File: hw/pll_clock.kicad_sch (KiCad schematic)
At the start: 21 parts, among them J7 BNC, U7 5P49V5925, Y1 25MHz

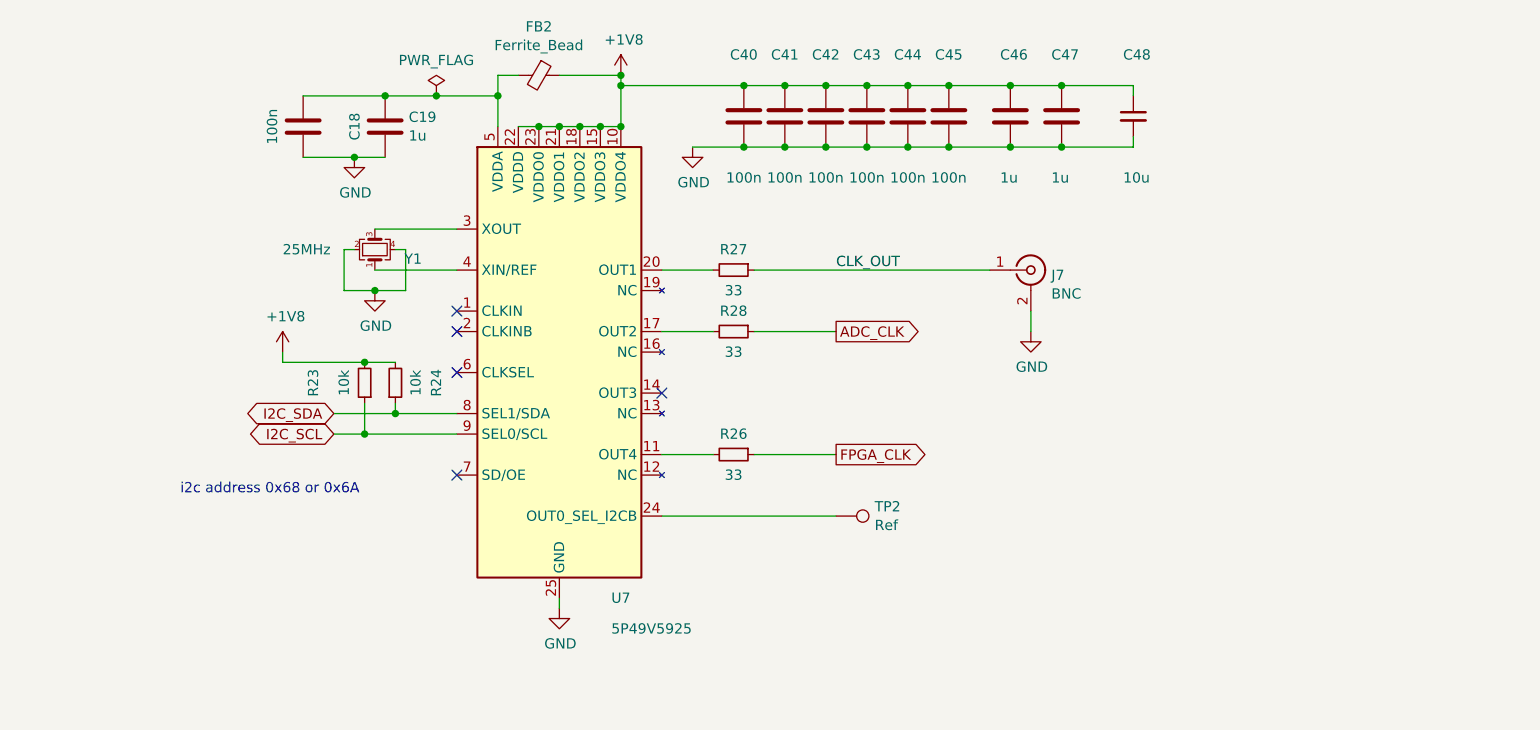
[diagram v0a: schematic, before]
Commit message: basic schematic, started layout (placing first components)
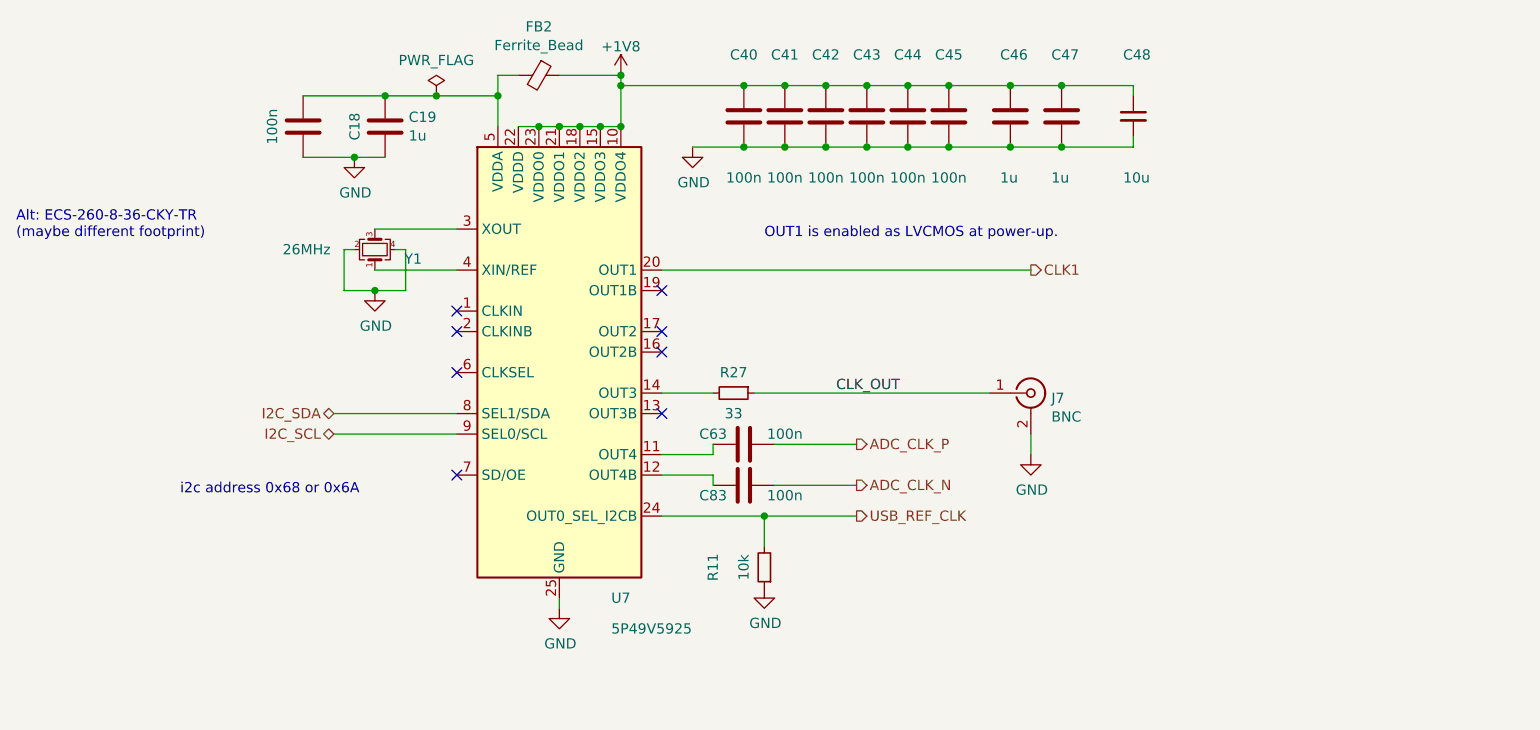
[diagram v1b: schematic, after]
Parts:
- removed R23, R24: 10k, Resistor_SMD:R_0603_1608Metric, symbol Device:R_Small
- removed R26, R28: 33, Resistor_SMD:R_0603_1608Metric, symbol Device:R_Small
- removed TP2: Ref, proj_footprints:TestPoint_Pad_D0.8mm_no_CY, symbol Connector:TestPoint
- added C63, C83: 100n, Capacitor_SMD:C_0603_1608Metric, symbol fmc:100nF_603
- added R11: 10k, Resistor_SMD:R_0603_1608Metric, symbol Device:R_Small
- FB2: symbol usbadc-rescue:Ferrite_Bead_Small-Device -> Device:FerriteBead_Small
- U7: symbol fmc:5P49V5925 -> Oscillator:5P49V6965
- Y1: value 25MHz -> 26MHz; Part ABM10W-25.0000MHZ-8-B1U-T3 -> ABM10W-26.0000MHZ-8-B1U-T3
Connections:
- net GND: now also R11.1
- net at R27.2: now also U7.14 (OUT3); no longer U7.20 (OUT1)
- net at U7.11 (OUT4): now also C63.2
- net at U7.12 (OUT4B): now also C83.2
- net USB_REF_CLK: now reaches U7.24 (OUT0_SEL_I2CB)
- net USB_REF_CLK: now also R11.2
- new net ADC_CLK_N: C83.1
- new net ADC_CLK_P: C63.1
- new net CLK1: U7.20 (OUT1)
- no-connect marks 5 -> 8
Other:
- note added: "Alt: ECS-260-8-36-CKY-TR (maybe different footprint)"
- note added: "OUT1 is enabled as LVCMOS at power-up."
- moved on the sheet: J7, R27

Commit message: WIP - a lot already laid out.
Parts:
- added R24: 33, Resistor_SMD:R_0603_1608Metric, symbol Device:R_Small
- added TP1: GND, usbadc_local:single_pad, symbol Connector:TestPoint_Small
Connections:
- net CLK1: now also R24.1; no longer U7.20 (OUT1)
- net GND: now also TP1.1
- net at R27.2: now also U7.17 (OUT2); no longer U7.14 (OUT3)
- net at U7.11 (OUT4): no longer C63.2
- net at U7.12 (OUT4B): no longer C83.2
- net at U7.13 (OUT3B): now also C83.2
- new net: C63.2, U7.14 (OUT3)
- new net: R24.2, U7.20 (OUT1)
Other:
- moved on the sheet: C63, C83, J7, R27

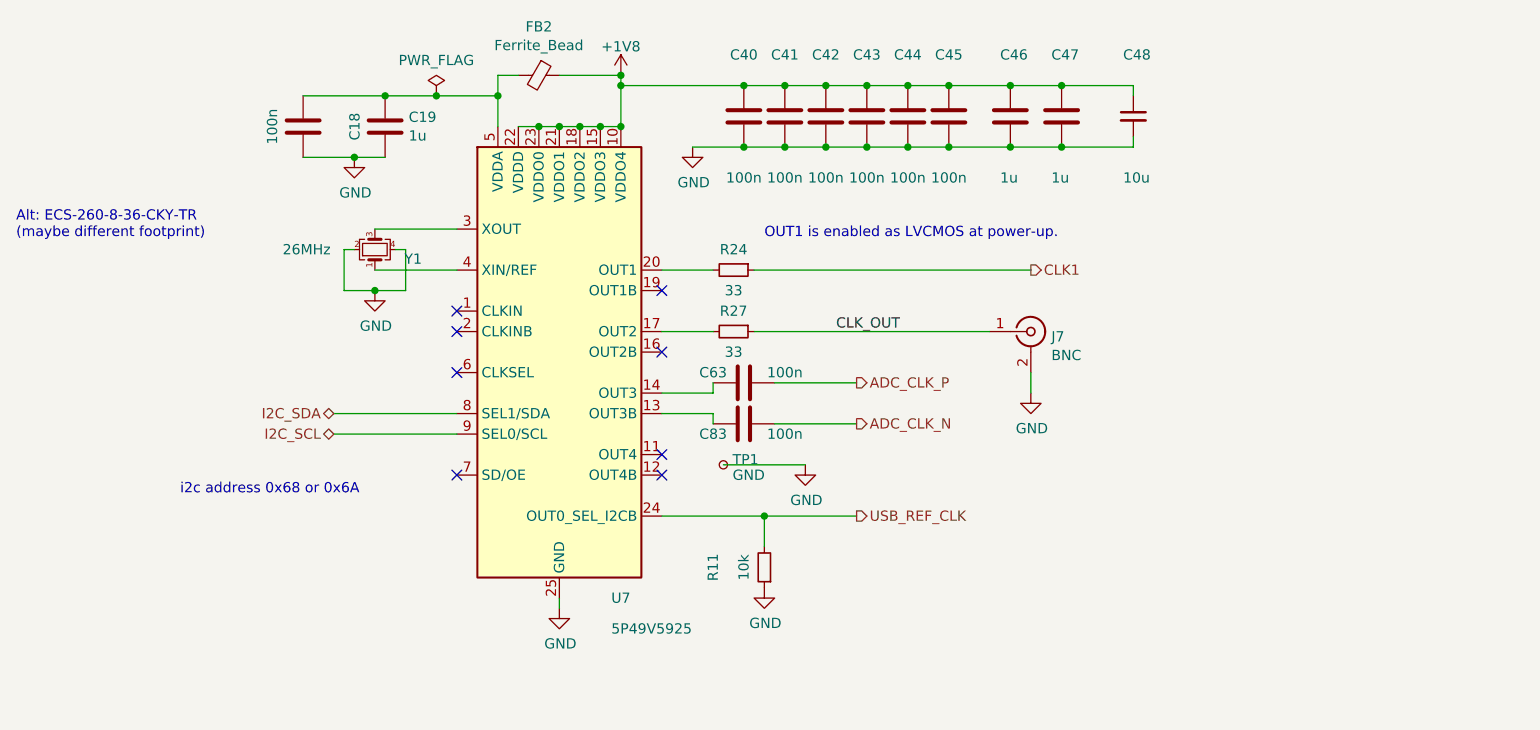
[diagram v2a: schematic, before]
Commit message: WIP - almost everything except power (converters) connected
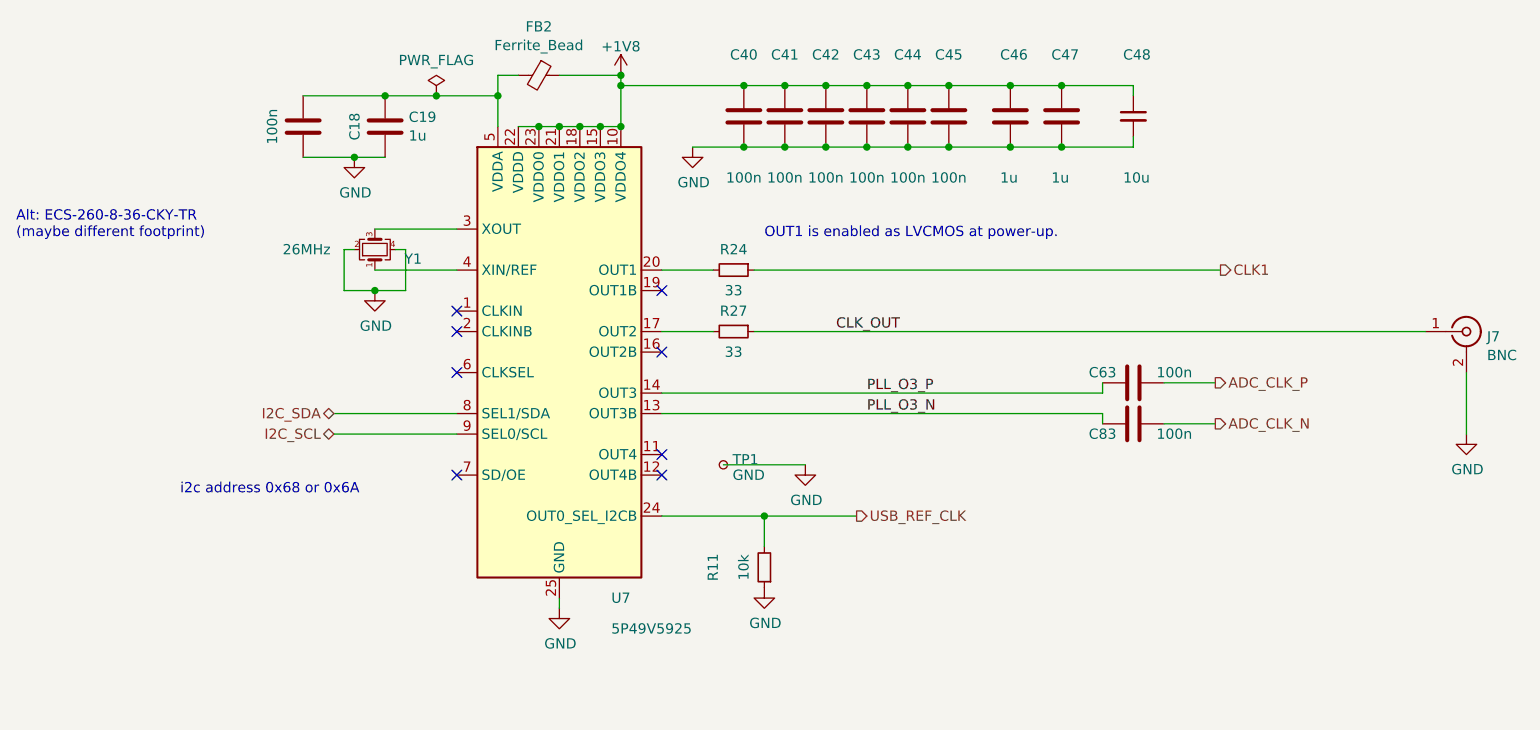
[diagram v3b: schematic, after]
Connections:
- net PLL_O3_N: now reaches C83.2, U7.13 (OUT3B)
- net PLL_O3_P: now reaches C63.2, U7.14 (OUT3)
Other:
- moved on the sheet: C63, C83, J7
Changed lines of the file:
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@@
   (no_connect (at 154.94 76.2))
   (no_connect (at 154.94 99.06))
-  (wire (pts (xy 161.29 91.44) (xy 161.29 92.71))
+  (wire (pts (xy 209.55 91.44) (xy 209.55 92.71))
     (stroke (width 0) (type default))
   )
@@
     (stroke (width 0) (type default))
   )
-  (wire (pts (xy 166.37 73.66) (xy 200.66 73.66))
+  (wire (pts (xy 166.37 73.66) (xy 224.155 73.66))
     (stroke (width 0) (type default))
   )
@@
     (stroke (width 0) (type default))
   )
-  (wire (pts (xy 200.66 86.36) (xy 200.66 88.9))
+  (wire (pts (xy 254.635 86.36) (xy 254.635 93.98))
     (stroke (width 0) (type default))
   )
@@
     (stroke (width 0) (type default))
   )
+  (wire (pts (xy 154.94 88.9) (xy 209.55 88.9))
+    (stroke (width 0) (type default))
+  )
   (wire (pts (xy 154.94 81.28) (xy 161.29 81.28))
     (stroke (width 0) (type default))
@@
     (stroke (width 0) (type default))
   )
-  (wire (pts (xy 154.94 88.9) (xy 161.29 88.9))
-    (stroke (width 0) (type default))
-  )
   (wire (pts (xy 120.65 59.69) (xy 116.84 59.69))
     (stroke (width 0) (type default))
@@
     (stroke (width 0) (type default))
   )
-  (wire (pts (xy 168.91 87.63) (xy 179.07 87.63))
+  (wire (pts (xy 217.17 87.63) (xy 223.52 87.63))
     (stroke (width 0) (type default))
   )
@@
     (stroke (width 0) (type default))
   )
-  (wire (pts (xy 154.94 91.44) (xy 161.29 91.44))
+  (wire (pts (xy 154.94 91.44) (xy 209.55 91.44))
     (stroke (width 0) (type default))
   )
@@
     (stroke (width 0) (type default))
   )
-  (wire (pts (xy 168.91 92.71) (xy 179.07 92.71))
-    (stroke (width 0) (type default))
-  )
-  (wire (pts (xy 161.29 87.63) (xy 161.29 88.9))
+  (wire (pts (xy 217.17 92.71) (xy 223.52 92.71))
+    (stroke (width 0) (type default))
+  )
+  (wire (pts (xy 209.55 87.63) (xy 209.55 88.9))
     (stroke (width 0) (type default))
   )
@@
     (stroke (width 0) (type default))
   )
-  (wire (pts (xy 166.37 81.28) (xy 195.58 81.28))
+  (wire (pts (xy 166.37 81.28) (xy 249.555 81.28))
     (stroke (width 0) (type default))
   )
@@
     (effects (font (size 1.27 1.27)) (justify left bottom))
   )
+  (label "PLL_O3_P" (at 180.34 88.9 0) (fields_autoplaced)
+    (effects (font (size 1.27 1.27)) (justify left bottom))
+  )
+  (label "PLL_O3_N" (at 180.34 91.44 0) (fields_autoplaced)
+    (effects (font (size 1.27 1.27)) (justify left bottom))
+  )
   (label "CLK_OUT" (at 176.53 81.28 0) (fields_autoplaced)
     (effects (font (size 1.27 1.27)) (justify left bottom))
   )
-  (hierarchical_label "CLK1" (shape output) (at 200.66 73.66 0) (fields_autoplaced)
+  (hierarchical_label "CLK1" (shape output) (at 224.155 73.66 0) (fields_autoplaced)
     (effects (font (size 1.27 1.27)) (justify left))
   )
@@
     (effects (font (size 1.27 1.27)) (justify right))
   )
-  (hierarchical_label "ADC_CLK_N" (shape output) (at 179.07 92.71 0) (fields_autoplaced)
+  (hierarchical_label "ADC_CLK_N" (shape output) (at 223.52 92.71 0) (fields_autoplaced)
     (effects (font (size 1.27 1.27)) (justify left))
   )
@@
     (effects (font (size 1.27 1.27)) (justify right))
   )
-  (hierarchical_label "ADC_CLK_P" (shape output) (at 179.07 87.63 0) (fields_autoplaced)
+  (hierarchical_label "ADC_CLK_P" (shape output) (at 223.52 87.63 0) (fields_autoplaced)
     (effects (font (size 1.27 1.27)) (justify left))
   )
@@
     (effects (font (size 1.27 1.27)) (justify left))
   )
-  (symbol (lib_id "power:GND") (at 200.66 88.9 0) (unit 1)
-    (in_bom yes) (on_board yes) (dnp no)
-    (property "Reference" "#PWR?" (at 200.66 95.25 0)
-      (effects (font (size 1.27 1.27)) hide)
-    )
-    (property "Value" "GND" (at 200.787 93.2942 0)
-      (effects (font (size 1.27 1.27)))
-    )
-    (property "Footprint" "" (at 200.66 88.9 0)
-      (effects (font (size 1.27 1.27)) hide)
-    )
-    (property "Datasheet" "" (at 200.66 88.9 0)
+  (symbol (lib_id "power:GND") (at 254.635 93.98 0) (unit 1)
+    (in_bom yes) (on_board yes) (dnp no)
+    (property "Reference" "#PWR?" (at 254.635 100.33 0)
+      (effects (font (size 1.27 1.27)) hide)
+    )
+    (property "Value" "GND" (at 254.762 98.3742 0)
+      (effects (font (size 1.27 1.27)))
+    )
+    (property "Footprint" "" (at 254.635 93.98 0)
+      (effects (font (size 1.27 1.27)) hide)
+    )
+    (property "Datasheet" "" (at 254.635 93.98 0)
       (effects (font (size 1.27 1.27)) hide)
     )
@@
     )
   )
-  (symbol (lib_id "Connector:Conn_Coaxial") (at 200.66 81.28 0) (unit 1)
-    (in_bom yes) (on_board yes) (dnp no)
-    (property "Reference" "J7" (at 203.2 81.915 0)
-      (effects (font (size 1.27 1.27)) (justify left))
-    )
-    (property "Value" "BNC" (at 203.2 84.2264 0)
-      (effects (font (size 1.27 1.27)) (justify left))
-    )
-    (property "Footprint" "proj_footprints:BNC_Molex_0731713150" (at 200.66 81.28 0)
-      (effects (font (size 1.27 1.27)) hide)
-    )
-    (property "Datasheet" " ~" (at 200.66 81.28 0)
-      (effects (font (size 1.27 1.27)) hide)
-    )
-    (property "Part" "0731713150" (at 200.66 81.28 0)
-      (effects (font (size 1.27 1.27)) hide)
-    )
-    (property "Manufacturer" "Molex" (at 200.66 81.28 0)
+  (symbol (lib_id "Connector:Conn_Coaxial") (at 254.635 81.28 0) (unit 1)
+    (in_bom yes) (on_board yes) (dnp no)
+    (property "Reference" "J7" (at 257.175 81.915 0)
+      (effects (font (size 1.27 1.27)) (justify left))
+    )
+    (property "Value" "BNC" (at 257.175 84.2264 0)
+      (effects (font (size 1.27 1.27)) (justify left))
+    )
+    (property "Footprint" "proj_footprints:BNC_Molex_0731713150" (at 254.635 81.28 0)
+      (effects (font (size 1.27 1.27)) hide)
+    )
+    (property "Datasheet" " ~" (at 254.635 81.28 0)
+      (effects (font (size 1.27 1.27)) hide)
+    )
+    (property "Part" "0731713150" (at 254.635 81.28 0)
+      (effects (font (size 1.27 1.27)) hide)
+    )
+    (property "Manufacturer" "Molex" (at 254.635 81.28 0)
       (effects (font (size 1.27 1.27)) hide)
     )
@@
     )
   )
-  (symbol (lib_id "fmc:100nF_603") (at 165.1 87.63 270) (unit 1)
-    (in_bom yes) (on_board yes) (dnp no)
-    (property "Reference" "C63" (at 161.29 86.36 90)
-      (effects (font (size 1.27 1.27)))
-    )
-    (property "Value" "100n" (at 170.18 86.36 90)
-      (effects (font (size 1.27 1.27)))
-    )
-    (property "Footprint" "Capacitor_SMD:C_0603_1608Metric" (at 161.29 88.5952 0)
-      (effects (font (size 1.27 1.27)) hide)
-    )
-    (property "Datasheet" "~" (at 165.1 87.63 0)
-      (effects (font (size 1.27 1.27)) hide)
-    )
-    (property "Part" "GCJ188R71E104KA12D" (at 170.18 90.805 0)
-      (effects (font (size 1.27 1.27)) hide)
-    )
-    (property "Manufacturer" "Murata" (at 172.72 93.345 0)
+  (symbol (lib_id "fmc:100nF_603") (at 213.36 87.63 270) (unit 1)
+    (in_bom yes) (on_board yes) (dnp no)
+    (property "Reference" "C63" (at 209.55 86.36 90)
+      (effects (font (size 1.27 1.27)))
+    )
+    (property "Value" "100n" (at 218.44 86.36 90)
+      (effects (font (size 1.27 1.27)))
+    )
+    (property "Footprint" "Capacitor_SMD:C_0603_1608Metric" (at 209.55 88.5952 0)
+      (effects (font (size 1.27 1.27)) hide)
+    )
+    (property "Datasheet" "~" (at 213.36 87.63 0)
+      (effects (font (size 1.27 1.27)) hide)
+    )
+    (property "Part" "GCJ188R71E104KA12D" (at 218.44 90.805 0)
+      (effects (font (size 1.27 1.27)) hide)
+    )
+    (property "Manufacturer" "Murata" (at 220.98 93.345 0)
       (effects (font (size 1.27 1.27)) hide)
     )
@@
     )
   )
-  (symbol (lib_id "fmc:100nF_603") (at 165.1 92.71 270) (mirror x) (unit 1)
-    (in_bom yes) (on_board yes) (dnp no)
-    (property "Reference" "C83" (at 161.29 93.98 90)
-      (effects (font (size 1.27 1.27)))
-    )
-    (property "Value" "100n" (at 170.18 93.98 90)
-      (effects (font (size 1.27 1.27)))
-    )
-    (property "Footprint" "Capacitor_SMD:C_0603_1608Metric" (at 161.29 91.7448 0)
-      (effects (font (size 1.27 1.27)) hide)
-    )
-    (property "Datasheet" "~" (at 165.1 92.71 0)
-      (effects (font (size 1.27 1.27)) hide)
-    )
-    (property "Part" "GCJ188R71E104KA12D" (at 170.18 89.535 0)
-      (effects (font (size 1.27 1.27)) hide)
-    )
-    (property "Manufacturer" "Murata" (at 172.72 86.995 0)
-      (effects (font (size 1.27 1.27)) hide)
-    )
+  (symbol (lib_id "fmc:100nF_603") (at 213.36 92.71 270) (mirror x) (unit 1)
+    (in_bom yes) (on_board yes) (dnp no)
+    (property "Reference" "C83" (at 209.55 93.98 90)
+      (effects (font (size 1.27 1.27)))
+    )
+    (property "Value" "100n" (at 218.44 93.98 90)
+      (effects (font (size 1.27 1.27)))
+    )
+    (property "Footprint" "Capacitor_SMD:C_0603_1608Metric" (at 209.55 91.7448 0)
+      (effects (font (size 1.27 1.27)) hide)
+    )
+    (property "Datasheet" "~" (at 213.36 92.71 0)
+      (effects (font (size 1.27 1.27)) hide)
+    )
+    (property "Part" "GCJ188R71E104KA12D" (at 218.44 89.535 0)
+      (effects (font (size 1.27 1.27)) hide)
+    )
+    (property "Manufacturer" "Murata" (at 220.98 86.995 0)
+      (effects (font (size 1.27 1.27)) hide)
+    )
